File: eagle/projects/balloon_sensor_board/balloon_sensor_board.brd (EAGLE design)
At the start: 18.1 x 13.2 mm, 13 parts, among them J201 MOL-SL-4-RA, U1 PCT2075GVJ, U202 MS560702BA03-50

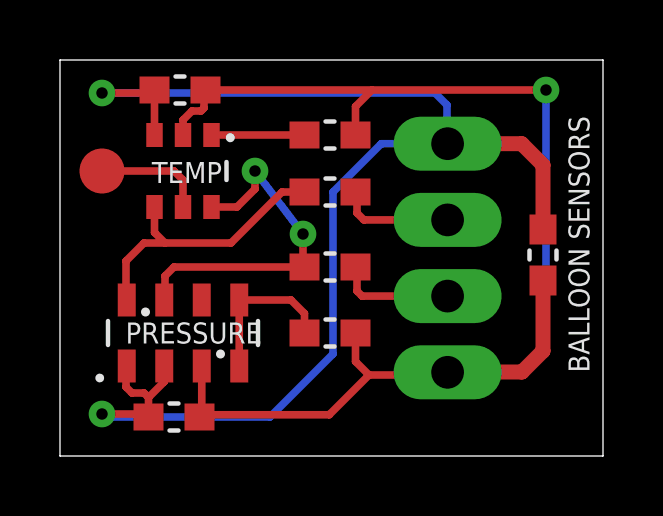
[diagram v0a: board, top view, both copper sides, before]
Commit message: somehow PP3V3_HAT got renamed to NFO???
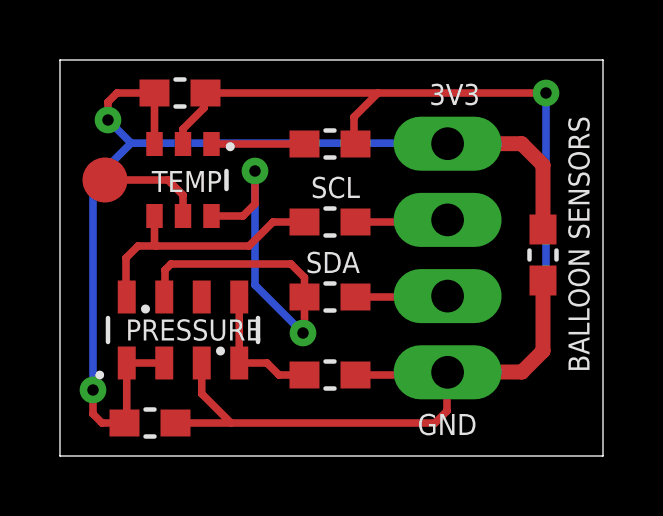
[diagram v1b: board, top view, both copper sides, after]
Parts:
- moved R204 1.40 mm to (9.00, 2.70)
- moved LOGO1 1.39 mm to (9.30, 0.40)
- moved R201 1.00 mm to (9.00, 7.80)
- moved R202 1.00 mm to (9.00, 5.30)
- moved C203 0.82 mm to (3.00, 1.10)
- moved TP201 0.32 mm to (1.50, 9.20)
- moved U1 0.30 mm to (4.10, 9.20)
- moved R203 0.30 mm to (9.00, 10.4)
- moved U202 0.10 mm to (4.10, 4.20)
- moved C202 0.10 mm to (4.00, 12.1)
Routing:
- net PP3V3: track 45.5 -> 35.3 mm
- net I2C_SDA: track 11.6 -> 16.5 mm
- net GND: track 45.3 -> 49.5 mm
- net I2C_SDA_COMM: track 3.91 -> 3.08 mm
- net I2C_SCL: track 9.56 -> 8.78 mm
- net I2C_SCL_CONN: track 3.84 -> 3.10 mm
- net PRES0_CSB: track 5.21 -> 4.54 mm
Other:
- board text added: "3V3"
- board text added: "GND"
- board text added: "SCL"
- board text added: "SDA"

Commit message: cleaned up HAT and balloon_sensor for panelling
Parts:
- added TP202: (no value), daqcs:TP15R
- moved TP201 16.2 mm to (15.6, 1.30)
- renumbered LOGO1 to LOGO201, LOGO2 to LOGO202, U1 to U201
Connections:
- net GND: now also TP201.TP
- net TEMP0_OS: now also TP202.TP; no longer TP201.TP
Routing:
- net GND: track 49.5 -> 52.3 mm
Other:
- board text added: "CHRIS SCHWAB P17105: HABIP SPRING 2017 002-004-01"
- board text removed: "CHRIS SCHWAB P17105: HABIP SPRING 2017 XXX-XXX-XX"
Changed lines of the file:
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@@
 P17105: HABIP
 SPRING 2017
-XXX-XXX-XX</text>
+002-004-01</text>
 <text x="5.4" y="9.5" size="0.7" layer="21" ratio="22" rot="R180">TEMP</text>
 <text x="6.73" y="4.55" size="0.7" layer="21" ratio="22" rot="R180">PRESSURE</text>
@@
 </variantdefs>
 <classes>
-<class number="0" name="default" width="0" drill="0">
+<class number="0" name="default" width="0" drill="0.381">
+<clearance class="0" value="0.1524"/>
 </class>
 </classes>
@@
 <attribute name="POWER" value="1/10W" x="14.08" y="14.21" size="1.778" layer="27" rot="R180" display="off"/>
 </element>
-<element name="TP201" library="daqcs" package="TP15R" value="" x="1.5" y="9.2" smashed="yes">
+<element name="TP202" library="daqcs" package="TP15R" value="" x="1.5" y="9.2" smashed="yes">
 <attribute name="TP_SIGNAL_NAME" value="" x="1.5" y="7.595" size="0.4064" layer="37" ratio="6"/>
 <attribute name="VALUE" x="2.019" y="8.192" size="0.254" layer="27" ratio="6"/>
 </element>
-<element name="U1" library="daqcs" package="TSOP95P080X055-6N" value="PCT2075GVJ" x="4.1" y="9.2" smashed="yes" rot="R270">
+<element name="U201" library="daqcs" package="TSOP95P080X055-6N" value="PCT2075GVJ" x="4.1" y="9.2" smashed="yes" rot="R270">
 <attribute name="DATASHEET" value="HW/docs/projects/raspi_zero_power_sensor_hat/datasheets/sensors/PCT2075.pdf" x="4.1" y="9.2" size="1.778" layer="27" rot="R270" display="off"/>
 <attribute name="VENDOR_PN" value="568-12424-1-ND" x="4.1" y="9.2" size="1.778" layer="27" rot="R270" display="off"/>
@@
 <attribute name="INTERFACE" value="I2C" x="4.1" y="9.2" size="1.778" layer="27" rot="R270" display="off"/>
 </element>
-<element name="LOGO1" library="daqcs" package="SQUAD_LOGO" value="" x="9.3" y="0.4" rot="MR0">
+<element name="LOGO201" library="daqcs" package="SQUAD_LOGO" value="" x="9.3" y="0.4" rot="MR0">
 <attribute name="_EXTERNAL_" value="" x="9.3" y="0.4" size="1.778" layer="28" rot="MR0" display="off"/>
 </element>
-<element name="LOGO2" library="daqcs" package="CMS_LOGO" value="" x="17.1" y="1" rot="MR0"/>
+<element name="LOGO202" library="daqcs" package="CMS_LOGO" value="" x="17.1" y="1" rot="MR0"/>
+<element name="TP201" library="daqcs" package="TP15R" value="" x="15.6" y="1.3" smashed="yes">
+<attribute name="TP_SIGNAL_NAME" value="" x="15.6" y="-0.305" size="0.4064" layer="37" ratio="6"/>
+<attribute name="VALUE" x="16.119" y="0.292" size="0.254" layer="27" ratio="6"/>
+</element>
 </elements>
 <signals>
@@
 <contactref element="C202" pad="1"/>
 <contactref element="R203" pad="1"/>
-<contactref element="U1" pad="2"/>
+<contactref element="U201" pad="2"/>
 <via x="16.2" y="12.1" extent="1-16" drill="0.381"/>
 <wire x1="4.8" y1="12.15" x2="4.85" y2="12.1" width="0.254" layer="1"/>
@@
 <wire x1="12.9" y1="2.77" x2="12.92" y2="2.79" width="0.254" layer="1"/>
 <wire x1="3.85" y1="1.1" x2="5.7" y2="1.1" width="0.254" layer="1"/>
+<contactref element="TP201" pad="TP"/>
+<wire x1="15.6" y1="1.3" x2="13.1" y2="1.3" width="0.254" layer="1"/>
+<wire x1="13.1" y1="1.3" x2="12.9" y2="1.5" width="0.254" layer="1"/>
 </signal>
 <signal name="PP3V3">
@@
 <contactref element="C203" pad="2"/>
 <contactref element="U202" pad="2"/>
-<contactref element="U1" pad="3"/>
+<contactref element="U201" pad="3"/>
 <via x="1.1" y="2.2" extent="1-16" drill="0.381"/>
 <via x="1.6" y="11.2" extent="1-16" drill="0.381"/>
@@
 <wire x1="2.225" y1="3.1" x2="2.225" y2="1.175" width="0.254" layer="1"/>
 <wire x1="2.225" y1="1.175" x2="2.15" y2="1.1" width="0.254" layer="1"/>
-<wire x1="12.9" y1="10.43" x2="2.37" y2="10.43" width="0.254" layer="16"/>
 <wire x1="2.37" y1="10.43" x2="1.6" y2="11.2" width="0.254" layer="16"/>
 <wire x1="1.1" y1="2.2" x2="1.1" y2="9.16" width="0.254" layer="16"/>
 <wire x1="1.1" y1="9.16" x2="2.37" y2="10.43" width="0.254" layer="16"/>
 <wire x1="1.1" y1="1.4" x2="1.1" y2="2.2" width="0.254" layer="1"/>
-<wire x1="12.9" y1="10.43" x2="12.92" y2="10.41" width="0" layer="19" extent="16-16"/>
+<wire x1="2.37" y1="10.43" x2="12.9" y2="10.43" width="0.254" layer="16"/>
+<wire x1="12.9" y1="10.43" x2="12.92" y2="10.41" width="0.254" layer="16"/>
 </signal>
 <signal name="I2C_SCL_CONN">
@@
 <contactref element="R201" pad="2"/>
 <contactref element="U202" pad="8"/>
-<contactref element="U1" pad="4"/>
+<contactref element="U201" pad="4"/>
 <wire x1="7.1" y1="7.8" x2="6.3" y2="7" width="0.254" layer="1"/>
 <wire x1="6.3" y1="7" x2="3.2" y2="7" width="0.254" layer="1"/>
@@
 <contactref element="R202" pad="2"/>
 <contactref element="U202" pad="7"/>
-<contactref element="U1" pad="6"/>
+<contactref element="U201" pad="6"/>
 <via x="8.1" y="4.1" extent="1-16" drill="0.381"/>
 <via x="6.5" y="9.5" extent="1-16" drill="0.381"/>
@@
 <signal name="TEMP0_I2C_A0">
 <contactref element="R203" pad="2"/>
-<contactref element="U1" pad="1"/>
+<contactref element="U201" pad="1"/>
 <wire x1="5.05" y1="10.4" x2="8.15" y2="10.4" width="0.254" layer="1"/>
 </signal>
 <signal name="TEMP0_OS">
-<contactref element="TP201" pad="TP"/>
-<contactref element="U1" pad="5"/>
+<contactref element="TP202" pad="TP"/>
+<contactref element="U201" pad="5"/>
 <wire x1="4.1" y1="8" x2="4.1" y2="8.7" width="0.254" layer="1"/>
 <wire x1="4.1" y1="8.7" x2="3.6" y2="9.2" width="0.254" layer="1"/>
